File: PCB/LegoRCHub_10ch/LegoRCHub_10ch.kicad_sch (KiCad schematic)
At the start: 37 parts, among them J1 Conn_01x02, J10 Conn_01x03, J11 Conn_01x03_MountingPin, J12 Conn_01x02, J13 Conn_01x02, J2 Conn_01x02, J3 Conn_01x02, J4 Conn_01x02, J5 Conn_01x02, J6 Conn_01x02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

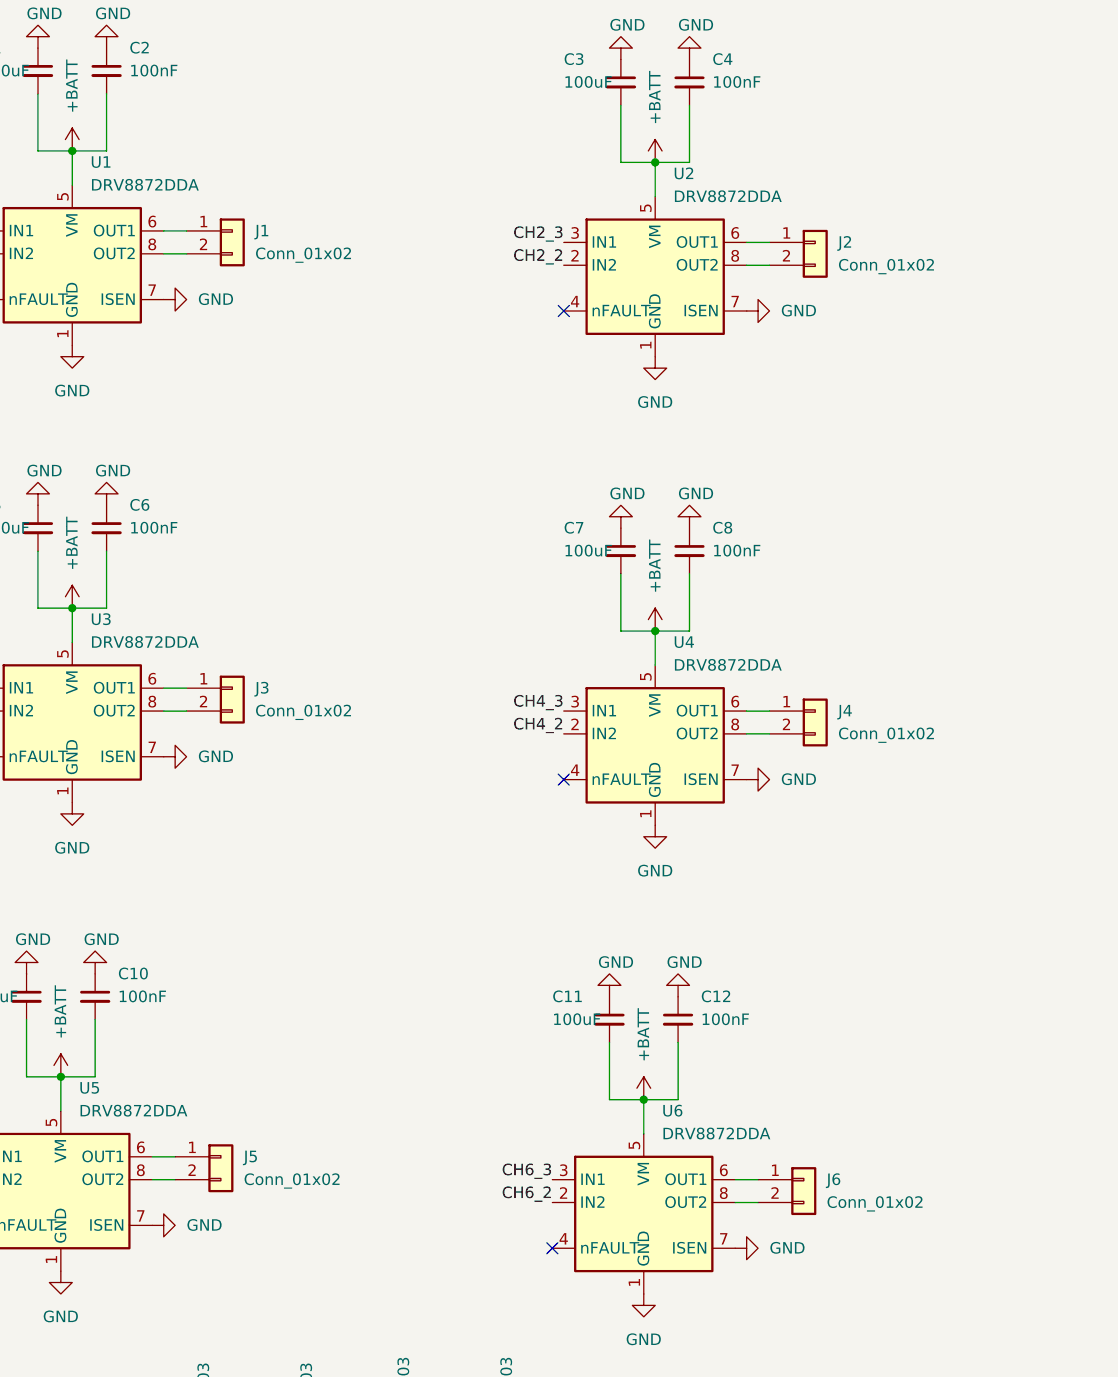
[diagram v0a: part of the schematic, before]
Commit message: Added project LegoRCHub_10ch: (beta 2): changed pins to screw terminals
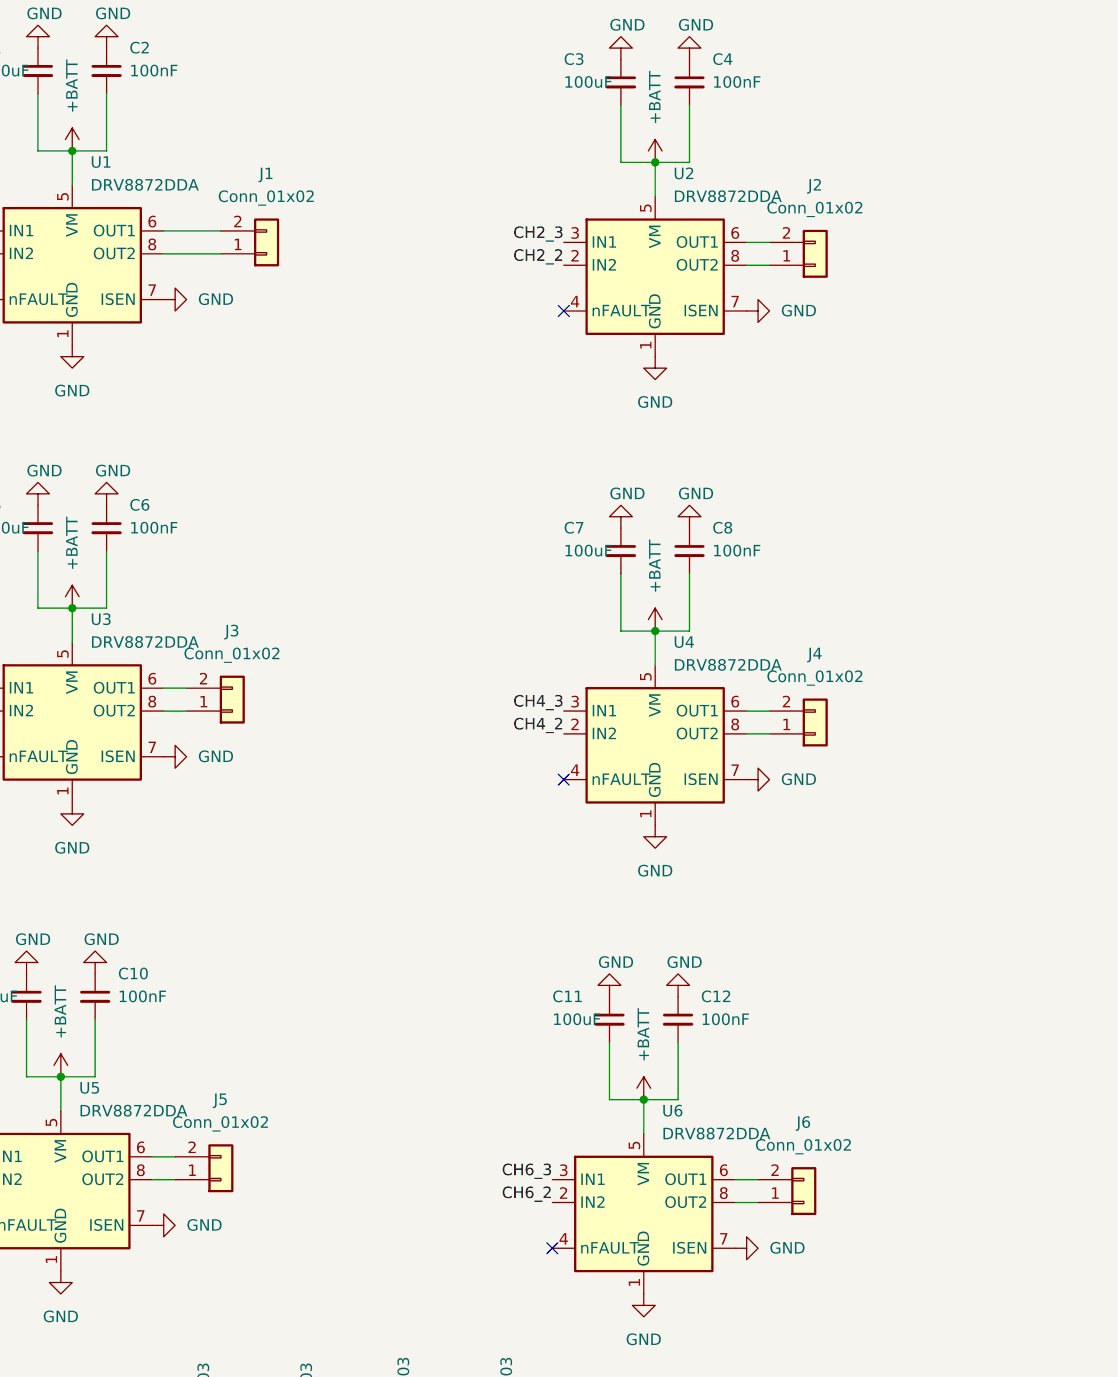
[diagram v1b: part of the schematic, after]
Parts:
- J1, J2, J3, J4, J5, J6: footprint Connector_PinHeader_2.54mm:PinHeader_1x02_P2.54mm_Vertical -> TerminalBlock_Phoenix:TerminalBlock_Phoenix_MPT-0,5-2-2.54_1x02_P2.54mm_Horizontal
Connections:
- net at U6.6 (OUT1): now also J6.2 (Pin_2); no longer J6.1 (Pin_1)
- net at U6.8 (OUT2): now also J6.1 (Pin_1); no longer J6.2 (Pin_2)
- net at J2.1 (Pin_1): now also U2.8 (OUT2); no longer U2.6 (OUT1)
- net at J2.2 (Pin_2): now also U2.6 (OUT1); no longer U2.8 (OUT2)
- net at J4.1 (Pin_1): now also U4.8 (OUT2); no longer U4.6 (OUT1)
- net at J4.2 (Pin_2): now also U4.6 (OUT1); no longer U4.8 (OUT2)
- net at U1.6 (OUT1): now also J1.2 (Pin_2); no longer J1.1 (Pin_1)
- net at U1.8 (OUT2): now also J1.1 (Pin_1); no longer J1.2 (Pin_2)
- net at J5.1 (Pin_1): now also U5.8 (OUT2); no longer U5.6 (OUT1)
- net at J5.2 (Pin_2): now also U5.6 (OUT1); no longer U5.8 (OUT2)
- net at J3.1 (Pin_1): now also U3.8 (OUT2); no longer U3.6 (OUT1)
- net at J3.2 (Pin_2): now also U3.6 (OUT1); no longer U3.8 (OUT2)
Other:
- moved on the sheet: J1
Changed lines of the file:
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@@
     (stroke (width 0) (type default) (color 0 0 0 0))
   )
-  (wire (pts (xy 52.07 43.18) (xy 54.61 43.18))
+  (wire (pts (xy 52.07 43.18) (xy 58.42 43.18))
     (stroke (width 0) (type default) (color 0 0 0 0))
   )
@@
     (stroke (width 0) (type default) (color 0 0 0 0))
   )
-  (wire (pts (xy 52.07 45.72) (xy 54.61 45.72))
+  (wire (pts (xy 52.07 45.72) (xy 58.42 45.72))
     (stroke (width 0) (type default) (color 0 0 0 0))
   )
@@
     (pin "1")
   )
-  (symbol (lib_id "Connector_Generic:Conn_01x02") (at 124.46 44.45 0) (unit 1)
-    (in_bom yes) (on_board yes) (fields_autoplaced)
-    (property "Reference" "J2" (id 0) (at 127 44.4499 0)
-      (effects (font (size 1.27 1.27)) (justify left))
-    )
-    (property "Value" "Conn_01x02" (id 1) (at 127 46.9899 0)
-      (effects (font (size 1.27 1.27)) (justify left))
-    )
-    (property "Footprint" "Connector_PinHeader_2.54mm:PinHeader_1x02_P2.54mm_Vertical" (id 2) (at 124.46 44.45 0)
-      (effects (font (size 1.27 1.27)) hide)
-    )
-    (property "Datasheet" "~" (id 3) (at 124.46 44.45 0)
+  (symbol (lib_id "Connector_Generic:Conn_01x02") (at 124.46 46.99 0) (mirror x) (unit 1)
+    (in_bom yes) (on_board yes) (fields_autoplaced)
+    (property "Reference" "J2" (id 0) (at 124.46 38.1 0))
+    (property "Value" "Conn_01x02" (id 1) (at 124.46 40.64 0))
+    (property "Footprint" "TerminalBlock_Phoenix:TerminalBlock_Phoenix_MPT-0,5-2-2.54_1x02_P2.54mm_Horizontal" (id 2) (at 124.46 46.99 0)
+      (effects (font (size 1.27 1.27)) hide)
+    )
+    (property "Datasheet" "~" (id 3) (at 124.46 46.99 0)
       (effects (font (size 1.27 1.27)) hide)
     )
@@
     (pin "1")
   )
-  (symbol (lib_id "Connector_Generic:Conn_01x02") (at 123.19 148.59 0) (unit 1)
-    (in_bom yes) (on_board yes) (fields_autoplaced)
-    (property "Reference" "J6" (id 0) (at 125.73 148.5899 0)
-      (effects (font (size 1.27 1.27)) (justify left))
-    )
-    (property "Value" "Conn_01x02" (id 1) (at 125.73 151.1299 0)
-      (effects (font (size 1.27 1.27)) (justify left))
-    )
-    (property "Footprint" "Connector_PinHeader_2.54mm:PinHeader_1x02_P2.54mm_Vertical" (id 2) (at 123.19 148.59 0)
-      (effects (font (size 1.27 1.27)) hide)
-    )
-    (property "Datasheet" "~" (id 3) (at 123.19 148.59 0)
+  (symbol (lib_id "Connector_Generic:Conn_01x02") (at 123.19 151.13 0) (mirror x) (unit 1)
+    (in_bom yes) (on_board yes) (fields_autoplaced)
+    (property "Reference" "J6" (id 0) (at 123.19 142.24 0))
+    (property "Value" "Conn_01x02" (id 1) (at 123.19 144.78 0))
+    (property "Footprint" "TerminalBlock_Phoenix:TerminalBlock_Phoenix_MPT-0,5-2-2.54_1x02_P2.54mm_Horizontal" (id 2) (at 123.19 151.13 0)
+      (effects (font (size 1.27 1.27)) hide)
+    )
+    (property "Datasheet" "~" (id 3) (at 123.19 151.13 0)
       (effects (font (size 1.27 1.27)) hide)
     )
@@
     (pin "2")
   )
-  (symbol (lib_id "Connector_Generic:Conn_01x02") (at 124.46 96.52 0) (unit 1)
-    (in_bom yes) (on_board yes) (fields_autoplaced)
-    (property "Reference" "J4" (id 0) (at 127 96.5199 0)
-      (effects (font (size 1.27 1.27)) (justify left))
-    )
-    (property "Value" "Conn_01x02" (id 1) (at 127 99.0599 0)
-      (effects (font (size 1.27 1.27)) (justify left))
-    )
-    (property "Footprint" "Connector_PinHeader_2.54mm:PinHeader_1x02_P2.54mm_Vertical" (id 2) (at 124.46 96.52 0)
-      (effects (font (size 1.27 1.27)) hide)
-    )
-    (property "Datasheet" "~" (id 3) (at 124.46 96.52 0)
+  (symbol (lib_id "Connector_Generic:Conn_01x02") (at 124.46 99.06 0) (mirror x) (unit 1)
+    (in_bom yes) (on_board yes) (fields_autoplaced)
+    (property "Reference" "J4" (id 0) (at 124.46 90.17 0))
+    (property "Value" "Conn_01x02" (id 1) (at 124.46 92.71 0))
+    (property "Footprint" "TerminalBlock_Phoenix:TerminalBlock_Phoenix_MPT-0,5-2-2.54_1x02_P2.54mm_Horizontal" (id 2) (at 124.46 99.06 0)
+      (effects (font (size 1.27 1.27)) hide)
+    )
+    (property "Datasheet" "~" (id 3) (at 124.46 99.06 0)
       (effects (font (size 1.27 1.27)) hide)
     )
@@
     (pin "9")
   )
-  (symbol (lib_id "Connector_Generic:Conn_01x02") (at 59.69 43.18 0) (unit 1)
-    (in_bom yes) (on_board yes) (fields_autoplaced)
-    (property "Reference" "J1" (id 0) (at 62.23 43.1799 0)
-      (effects (font (size 1.27 1.27)) (justify left))
-    )
-    (property "Value" "Conn_01x02" (id 1) (at 62.23 45.7199 0)
-      (effects (font (size 1.27 1.27)) (justify left))
-    )
-    (property "Footprint" "Connector_PinHeader_2.54mm:PinHeader_1x02_P2.54mm_Vertical" (id 2) (at 59.69 43.18 0)
-      (effects (font (size 1.27 1.27)) hide)
-    )
-    (property "Datasheet" "~" (id 3) (at 59.69 43.18 0)
+  (symbol (lib_id "Connector_Generic:Conn_01x02") (at 63.5 45.72 0) (mirror x) (unit 1)
+    (in_bom yes) (on_board yes) (fields_autoplaced)
+    (property "Reference" "J1" (id 0) (at 63.5 36.83 0))
+    (property "Value" "Conn_01x02" (id 1) (at 63.5 39.37 0))
+    (property "Footprint" "TerminalBlock_Phoenix:TerminalBlock_Phoenix_MPT-0,5-2-2.54_1x02_P2.54mm_Horizontal" (id 2) (at 63.5 45.72 0)
+      (effects (font (size 1.27 1.27)) hide)
+    )
+    (property "Datasheet" "~" (id 3) (at 63.5 45.72 0)
       (effects (font (size 1.27 1.27)) hide)
     )
@@
     (pin "2")
   )
-  (symbol (lib_id "Connector_Generic:Conn_01x02") (at 58.42 146.05 0) (unit 1)
-    (in_bom yes) (on_board yes) (fields_autoplaced)
-    (property "Reference" "J5" (id 0) (at 60.96 146.0499 0)
-      (effects (font (size 1.27 1.27)) (justify left))
-    )
-    (property "Value" "Conn_01x02" (id 1) (at 60.96 148.5899 0)
-      (effects (font (size 1.27 1.27)) (justify left))
-    )
-    (property "Footprint" "Connector_PinHeader_2.54mm:PinHeader_1x02_P2.54mm_Vertical" (id 2) (at 58.42 146.05 0)
-      (effects (font (size 1.27 1.27)) hide)
-    )
-    (property "Datasheet" "~" (id 3) (at 58.42 146.05 0)
+  (symbol (lib_id "Connector_Generic:Conn_01x02") (at 58.42 148.59 0) (mirror x) (unit 1)
+    (in_bom yes) (on_board yes) (fields_autoplaced)
+    (property "Reference" "J5" (id 0) (at 58.42 139.7 0))
+    (property "Value" "Conn_01x02" (id 1) (at 58.42 142.24 0))
+    (property "Footprint" "TerminalBlock_Phoenix:TerminalBlock_Phoenix_MPT-0,5-2-2.54_1x02_P2.54mm_Horizontal" (id 2) (at 58.42 148.59 0)
+      (effects (font (size 1.27 1.27)) hide)
+    )
+    (property "Datasheet" "~" (id 3) (at 58.42 148.59 0)
       (effects (font (size 1.27 1.27)) hide)
     )
@@
     (pin "1")
   )
-  (symbol (lib_id "Connector_Generic:Conn_01x02") (at 59.69 93.98 0) (unit 1)
-    (in_bom yes) (on_board yes) (fields_autoplaced)
-    (property "Reference" "J3" (id 0) (at 62.23 93.9799 0)
-      (effects (font (size 1.27 1.27)) (justify left))
-    )
-    (property "Value" "Conn_01x02" (id 1) (at 62.23 96.5199 0)
-      (effects (font (size 1.27 1.27)) (justify left))
-    )
-    (property "Footprint" "Connector_PinHeader_2.54mm:PinHeader_1x02_P2.54mm_Vertical" (id 2) (at 59.69 93.98 0)
-      (effects (font (size 1.27 1.27)) hide)
-    )
-    (property "Datasheet" "~" (id 3) (at 59.69 93.98 0)
+  (symbol (lib_id "Connector_Generic:Conn_01x02") (at 59.69 96.52 0) (mirror x) (unit 1)
+    (in_bom yes) (on_board yes) (fields_autoplaced)
+    (property "Reference" "J3" (id 0) (at 59.69 87.63 0))
+    (property "Value" "Conn_01x02" (id 1) (at 59.69 90.17 0))
+    (property "Footprint" "TerminalBlock_Phoenix:TerminalBlock_Phoenix_MPT-0,5-2-2.54_1x02_P2.54mm_Horizontal" (id 2) (at 59.69 96.52 0)
+      (effects (font (size 1.27 1.27)) hide)
+    )
+    (property "Datasheet" "~" (id 3) (at 59.69 96.52 0)
       (effects (font (size 1.27 1.27)) hide)
     )
@@
     )
     (path "/63237acf-d65e-4376-8010-e639fa624517"
-      (reference "J1") (unit 1) (value "Conn_01x02") (footprint "Connector_PinHeader_2.54mm:PinHeader_1x02_P2.54mm_Vertical")
+      (reference "J1") (unit 1) (value "Conn_01x02") (footprint "TerminalBlock_Phoenix:TerminalBlock_Phoenix_MPT-0,5-2-2.54_1x02_P2.54mm_Horizontal")
     )
     (path "/1cc895fb-07e8-4808-be3b-e9e84bc2a281"
-      (reference "J2") (unit 1) (value "Conn_01x02") (footprint "Connector_PinHeader_2.54mm:PinHeader_1x02_P2.54mm_Vertical")
+      (reference "J2") (unit 1) (value "Conn_01x02") (footprint "TerminalBlock_Phoenix:TerminalBlock_Phoenix_MPT-0,5-2-2.54_1x02_P2.54mm_Horizontal")
     )
     (path "/769b8617-07e6-4468-b6f1-8324d8f5fade"
-      (reference "J3") (unit 1) (value "Conn_01x02") (footprint "Connector_PinHeader_2.54mm:PinHeader_1x02_P2.54mm_Vertical")
+      (reference "J3") (unit 1) (value "Conn_01x02") (footprint "TerminalBlock_Phoenix:TerminalBlock_Phoenix_MPT-0,5-2-2.54_1x02_P2.54mm_Horizontal")
     )
     (path "/47767b78-bd8d-495e-b0b8-0f2ab5afce66"
-      (reference "J4") (unit 1) (value "Conn_01x02") (footprint "Connector_PinHeader_2.54mm:PinHeader_1x02_P2.54mm_Vertical")
+      (reference "J4") (unit 1) (value "Conn_01x02") (footprint "TerminalBlock_Phoenix:TerminalBlock_Phoenix_MPT-0,5-2-2.54_1x02_P2.54mm_Horizontal")
     )
     (path "/7300af46-ffd3-4251-804b-4563e8b6dacd"
-      (reference "J5") (unit 1) (value "Conn_01x02") (footprint "Connector_PinHeader_2.54mm:PinHeader_1x02_P2.54mm_Vertical")
+      (reference "J5") (unit 1) (value "Conn_01x02") (footprint "TerminalBlock_Phoenix:TerminalBlock_Phoenix_MPT-0,5-2-2.54_1x02_P2.54mm_Horizontal")
     )
     (path "/3613a043-186d-4759-8563-a19edbec2b7b"
-      (reference "J6") (unit 1) (value "Conn_01x02") (footprint "Connector_PinHeader_2.54mm:PinHeader_1x02_P2.54mm_Vertical")
+      (reference "J6") (unit 1) (value "Conn_01x02") (footprint "TerminalBlock_Phoenix:TerminalBlock_Phoenix_MPT-0,5-2-2.54_1x02_P2.54mm_Horizontal")
     )
     (path "/ab211755-b65b-4a34-9415-c412f22306fd"

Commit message: LegoRCHub_10ch: ...
Revert "LegoRCHub_10ch: ..."

This reverts commit a8209f8826470efcec7313ecef0b47345458ad62.
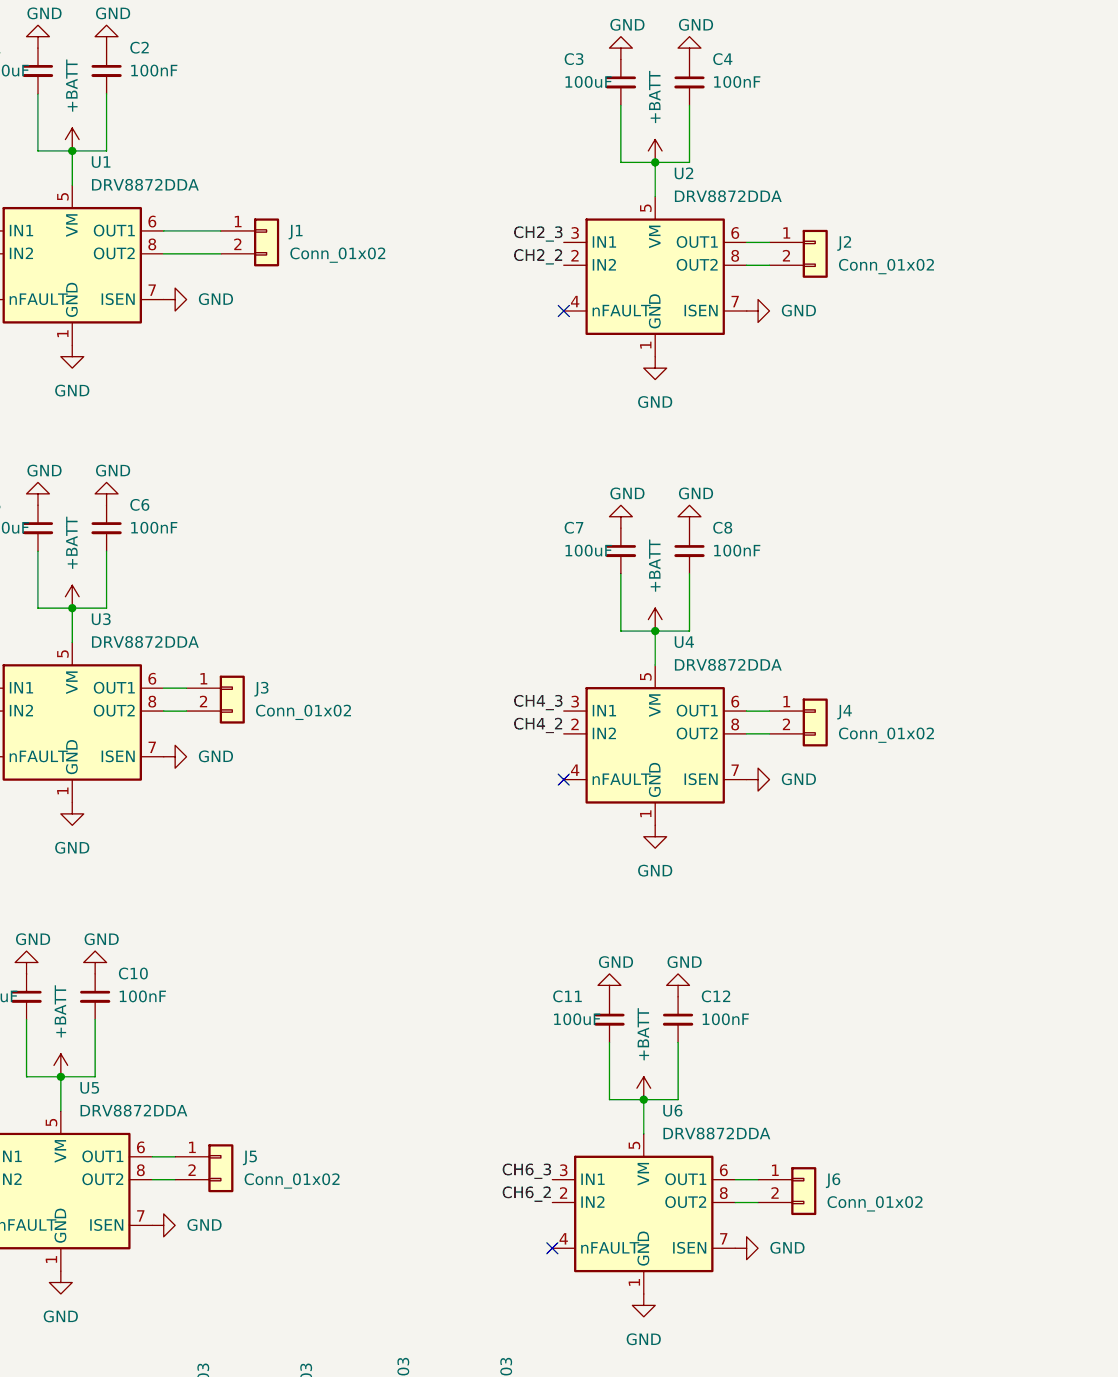
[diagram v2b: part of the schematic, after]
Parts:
- C13: footprint Capacitor_SMD:C_0805_2012Metric_Pad1.18x1.45mm_HandSolder -> Capacitor_SMD:C_1206_3216Metric_Pad1.33x1.80mm_HandSolder
- J1, J2, J3, J4, J5, J6: footprint TerminalBlock_Phoenix:TerminalBlock_Phoenix_MPT-0,5-2-2.54_1x02_P2.54mm_Horizontal -> Connector_Molex:Molex_KK-254_AE-6410-02A_1x02_P2.54mm_Vertical
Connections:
- net at U6.6 (OUT1): now also J6.1 (Pin_1); no longer J6.2 (Pin_2)
- net at U6.8 (OUT2): now also J6.2 (Pin_2); no longer J6.1 (Pin_1)
- net at J2.1 (Pin_1): now also U2.6 (OUT1); no longer U2.8 (OUT2)
- net at J2.2 (Pin_2): now also U2.8 (OUT2); no longer U2.6 (OUT1)
- net at J4.1 (Pin_1): now also U4.6 (OUT1); no longer U4.8 (OUT2)
- net at J4.2 (Pin_2): now also U4.8 (OUT2); no longer U4.6 (OUT1)
- net at U1.6 (OUT1): now also J1.1 (Pin_1); no longer J1.2 (Pin_2)
- net at U1.8 (OUT2): now also J1.2 (Pin_2); no longer J1.1 (Pin_1)
- net at J5.1 (Pin_1): now also U5.6 (OUT1); no longer U5.8 (OUT2)
- net at J5.2 (Pin_2): now also U5.8 (OUT2); no longer U5.6 (OUT1)
- net at J3.1 (Pin_1): now also U3.6 (OUT1); no longer U3.8 (OUT2)
- net at J3.2 (Pin_2): now also U3.8 (OUT2); no longer U3.6 (OUT1)
